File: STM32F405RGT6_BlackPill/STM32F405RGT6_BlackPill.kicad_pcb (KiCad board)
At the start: 2 copper layers, 57 parts, among them J100 Conn_01x04, J101 Conn_02x15_Odd_Even, J102 Conn_02x15_Odd_Even, J200 USB_C_Receptacle_USB2.0_16P, U100 STM32F405RGTx, U200 USBLC6-2SC6, U201 ACM2012-900-2P-T001, U300 TLV62569DBV, Y1 32768Hz, Y100 25Mhz

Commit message: Initial components placement
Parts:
- J100: footprint Connector_PinHeader_2.54mm:PinHeader_1x04_P2.54mm_Horizontal -> Connector_PinHeader_2.54mm:PinHeader_1x04_P2.54mm_Vertical
- L100, L300: value 10n -> 10nH
- moved SW101 140.4 mm to (76.1, 44.6)
- moved SW100 137.9 mm to (75.9, 60.8)
- moved SW102 133.3 mm to (82.5, 57.4), turned to 180 degrees
- moved U100 94.6 mm to (105.9, 54.7)
- moved R102 88.9 mm to (85.1, 49.7), turned to 90 degrees
- moved R107 87.8 mm to (85.0, 57.9), turned to -90 degrees
- moved Y1 87.7 mm to (90.0, 51.0), turned to 180 degrees
- moved Y100 86.8 mm to (90.0, 57.2), turned to 180 degrees
- moved R104 83.3 mm to (88.8, 54.5), turned to 180 degrees
- moved R100 82.7 mm to (84.9, 60.3), turned to 90 degrees
- moved C100 82.6 mm to (85.1, 47.5), turned to 90 degrees
- moved C113 82.3 mm to (88.8, 53.4)
- moved R103 81.2 mm to (89.0, 60.7), turned to 180 degrees
- moved C111 79.9 mm to (89.0, 59.6)
- moved C109 79.2 mm to (93.9, 56.9), turned to 90 degrees
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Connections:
- net Net-(C111-Pad1) renamed /MCU/XTAL_IN
- net Net-(C113-Pad1) renamed /MCU/XTAL32_IN
- net Net-(D101-A1) renamed /MCU/SWDIO_CONN
- net Net-(D102-A1) renamed /MCU/SWCLK_CONN
- net Net-(U100-VCAP_1) renamed /MCU/VCAP_1
- net Net-(U100-VCAP_2) renamed /MCU/VCAP_2
- C110 pad 1: HSE_OUT -> HSE_IN
- C112 pad 1: OSC32_OUT -> OSC32_IN
- R103 pad 1: HSE_IN -> HSE_OUT
- R104 pad 1: OSC32_IN -> OSC32_OUT
- Y1 pad 1: OSC32_OUT -> OSC32_IN
- Y100 pad 1: HSE_OUT -> HSE_IN
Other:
- copper layers 2 -> 4
- board text added: "BOOT0"
- board text added: "BTN PC13"
- board text added: "LED PB2"
- board text added: "NRST"

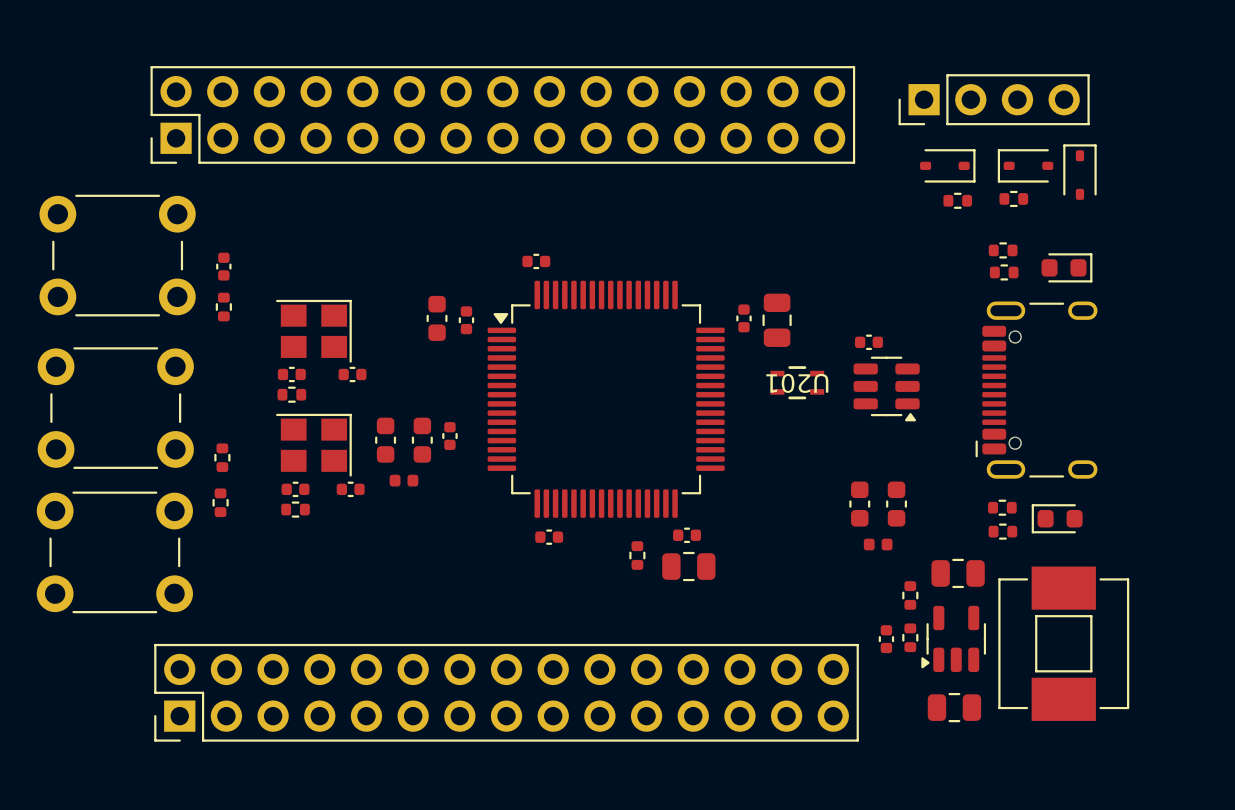
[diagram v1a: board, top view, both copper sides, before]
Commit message: Border outline
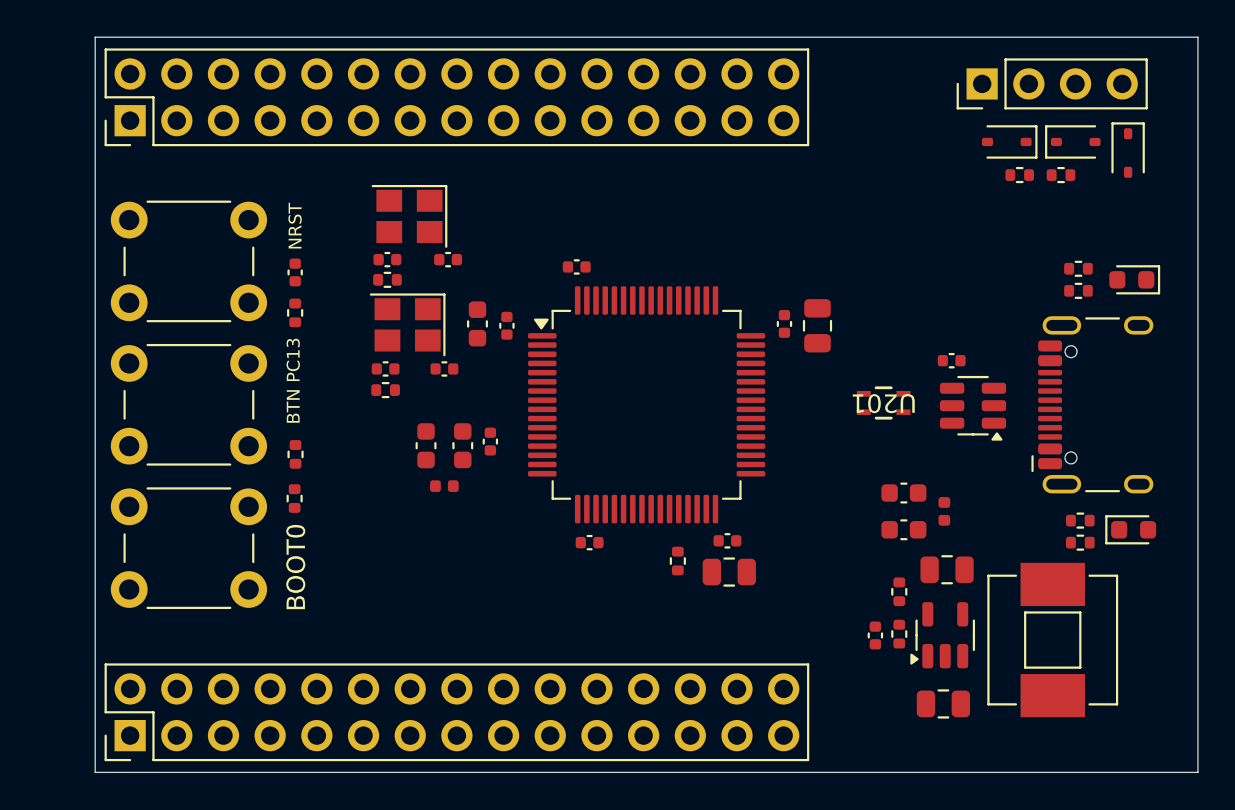
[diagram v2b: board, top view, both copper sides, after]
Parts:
- moved C110 8.30 mm to (97.1, 53.0)
- moved Y100 8.30 mm to (95.1, 50.6)
- moved C111 8.18 mm to (93.9, 53.0)
- moved R103 8.14 mm to (93.9, 54.2)
- moved C112 8.13 mm to (97.3, 47.1)
- moved C113 8.13 mm to (94.0, 47.1)
- moved R104 8.13 mm to (94.0, 48.2)
- moved Y1 8.13 mm to (95.2, 44.8)
- moved U201 4.83 mm to (121.0, 54.9)
- moved U200 4.82 mm to (125.9, 55.0)
- moved C200 4.61 mm to (124.7, 52.6)
- moved R201 4.30 mm to (131.7, 61.3)
- moved R302 4.26 mm to (131.7, 62.5)
- moved R108 4.22 mm to (131.6, 47.6)
- moved R200 4.16 mm to (131.6, 48.8)
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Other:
- board outline added: 60 x 40 mm

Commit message: Signal routing (bottom part)
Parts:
- moved SW101 22.0 mm to (79.8, 66.9), turned to 90 degrees
- moved SW100 18.0 mm to (84.2, 43.0), turned to -90 degrees
- moved R100 15.8 mm to (86.6, 44.5), turned to -90 degrees
- moved C100 15.7 mm to (86.6, 63.3)
- moved R102 15.7 mm to (86.6, 65.5)
- moved R201 12.6 mm to (131.6, 48.8)
- moved R200 12.5 mm to (131.7, 61.3)
- moved SW102 8.10 mm to (79.8, 52.7), turned to 0 degrees
- moved R107 5.61 mm to (88.5, 52.1)
- moved J102 4.40 mm to (84.4, 39.4)
- moved J101 4.38 mm to (84.4, 73.0)
- moved R101 3.47 mm to (109.4, 67.0), turned to 180 degrees
- moved R300 3.36 mm to (125.2, 67.8)
- moved C304 3.36 mm to (123.9, 67.8)
- moved L301 3.35 mm to (133.6, 67.9)
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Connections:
- C109 pad 1: +3V3 -> +3.3V
- C303 pad 1: +3V3 -> +3.3V
- C304 pad 1: +3V3 -> +3.3V
- D100 pad 1: +3V3 -> +3.3V
- D300 pad 2: +3V3 -> +3.3V
- J100 pad 4: +3V3 -> +3.3V
- J101 pad 1: +5V -> GND
- J101 pad 10: PC3 -> PA2
- J101 pad 11: PA0 -> PA5
- J101 pad 12: PA1 -> PA4
- J101 pad 13: PA2 -> PA7
- J101 pad 14: PA3 -> PA6
- J101 pad 15: PA4 -> PC5
- J101 pad 16: PA5 -> PC4
- J101 pad 17: PA6 -> PB1
- J101 pad 18: PA7 -> PB0
- J101 pad 19: PC4 -> PB11
- J101 pad 2: GND -> +3.3V
- J101 pad 20: PC5 -> PB10
- J101 pad 21: PB0 -> PB13
- J101 pad 22: PB1 -> PB12
- J101 pad 23: PB10 -> PB15
- J101 pad 24: PB11 -> PB14
- J101 pad 25: +3.3V -> PC7
- J101 pad 26: GND -> PC6
- J101 pad 27: +3.3V -> PC9
- J101 pad 28: GND -> PC8
- J101 pad 29: +3.3V -> GND
- J101 pad 3: +5V -> PC1
- J101 pad 30: GND -> +5V
- J101 pad 4: GND -> PC0
- J101 pad 5: +5V -> PC3
- J101 pad 6: GND -> PC2
- J101 pad 7: PC0 -> PA1
- J101 pad 8: PC1 -> PA0
- J101 pad 9: PC2 -> PA3
- J102 pad 19: PC9 -> unconnected-(J102-Pin_19-Pad19)
- J102 pad 20: PC8 -> unconnected-(J102-Pin_20-Pad20)
- J102 pad 21: PC7 -> unconnected-(J102-Pin_21-Pad21)
- J102 pad 22: PC6 -> unconnected-(J102-Pin_22-Pad22)
- J102 pad 23: PB15 -> unconnected-(J102-Pin_23-Pad23)
- J102 pad 24: PB14 -> unconnected-(J102-Pin_24-Pad24)
- J102 pad 25: PB13 -> unconnected-(J102-Pin_25-Pad25)
- J102 pad 26: PB12 -> unconnected-(J102-Pin_26-Pad26)
- L100 pad 2: +3V3 -> +3.3V
- L301 pad 2: +3V3 -> +3.3V
- R300 pad 2: +3V3 -> +3.3V
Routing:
- net +3.3V: track 0.00 -> 253.0 mm, vias 0 -> 12
- net PC13: track 0.00 -> 38.6 mm
- net BOOT0: track 0.00 -> 37.2 mm
- net NRST: track 0.00 -> 33.8 mm
- net GND: track 0.00 -> 32.5 mm, vias 0 -> 50
- net PC1: track 0.00 -> 30.2 mm
- net PC0: track 0.00 -> 28.4 mm
- net PC3: track 0.00 -> 27.9 mm
- net PC2: track 0.00 -> 25.9 mm
- net +5V: track 0.00 -> 25.9 mm
- net SWCLK: track 0.00 -> 24.7 mm
- net SWDIO: track 0.00 -> 24.0 mm
- net PC9: track 0.00 -> 23.9 mm
- net PC7: track 0.00 -> 22.8 mm
- net PA3: track 0.00 -> 22.7 mm
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- added copper zone on F.Cu, net +3.3V
- added copper zone on F.Cu, net +3.3VA
- added copper zone on F.Cu, net +5V
- added copper zone on F.Cu, net /power/BUCK_SW
- added copper zone on F.Cu, net GND
- added copper zone on In1.Cu, net GND
- added copper zone on In2.Cu, net GND
- added copper zone on F.Cu, net VBUS
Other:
- rule pad_to_mask_clearance: 0 -> 0.038

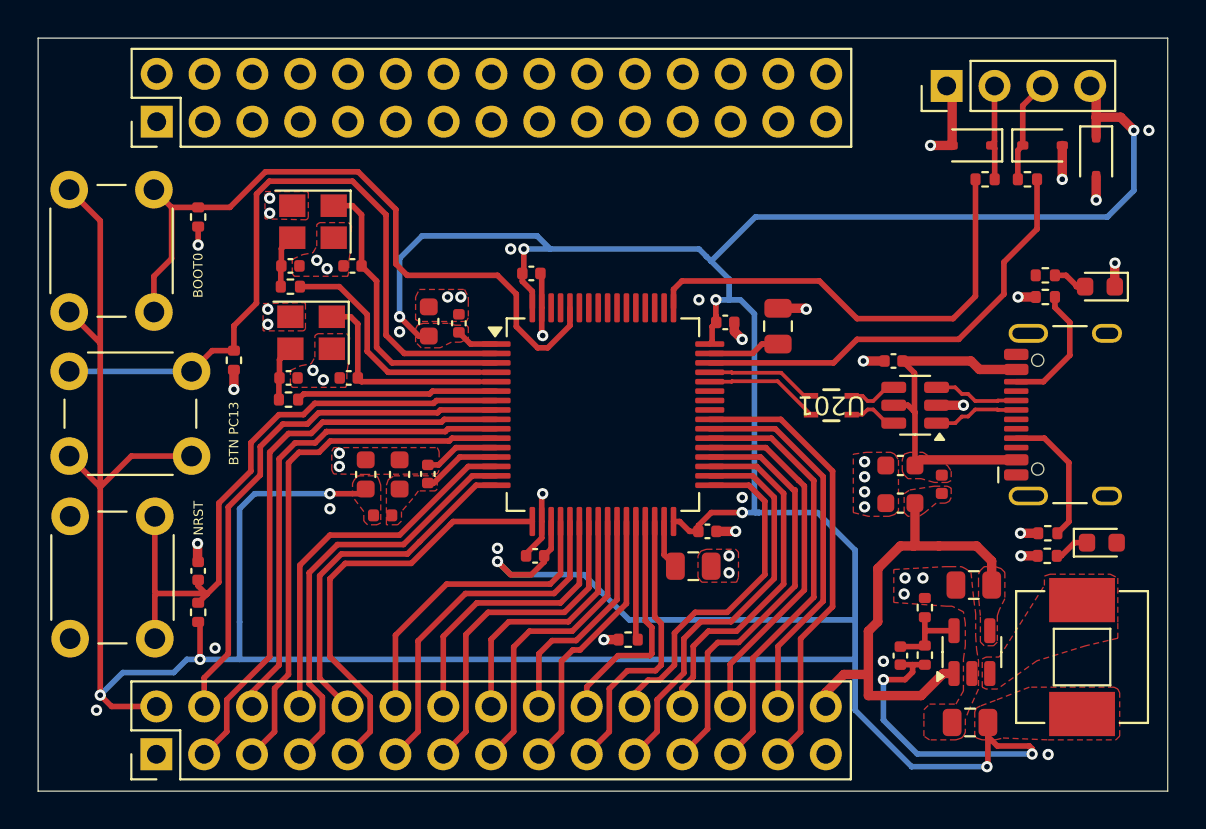
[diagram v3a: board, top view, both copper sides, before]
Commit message: Signal routing (upper part)
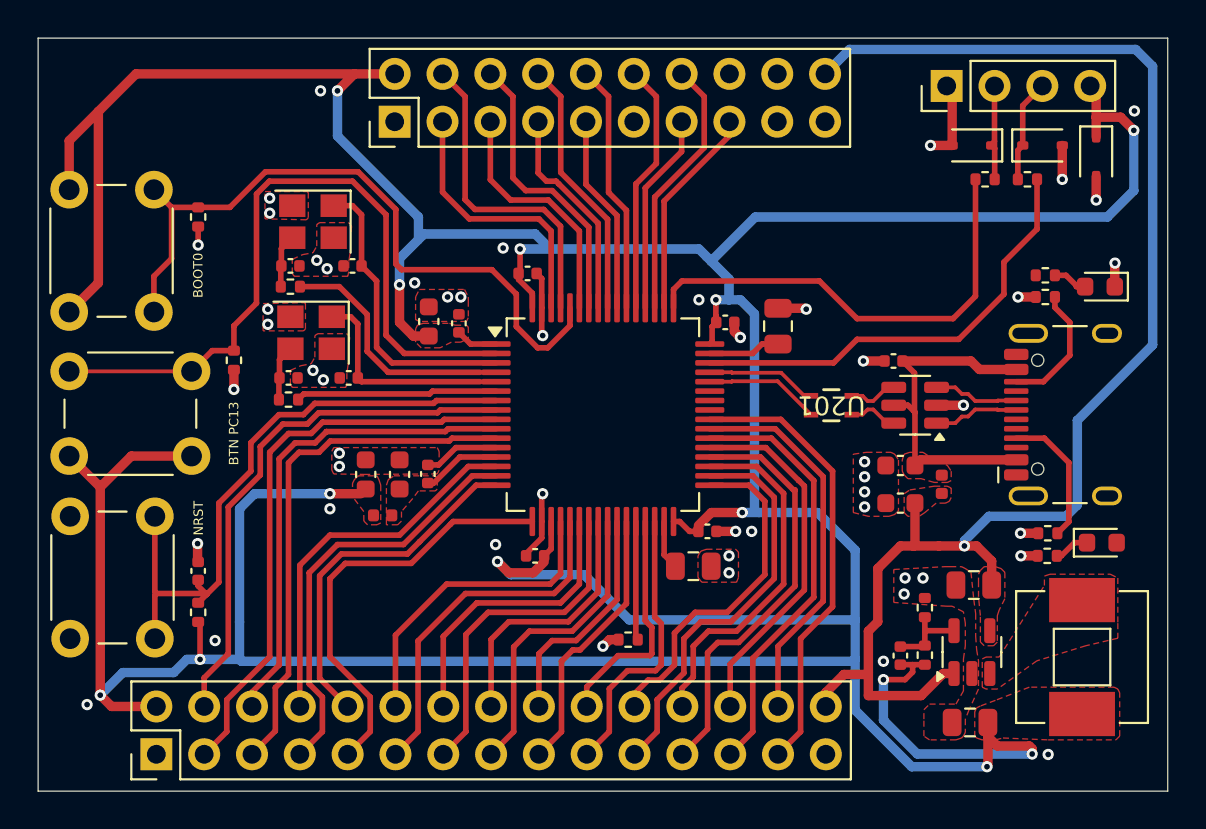
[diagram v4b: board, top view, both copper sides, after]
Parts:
- J102: value Conn_02x15_Odd_Even -> Conn_02x10_Odd_Even; footprint Connector_PinHeader_2.54mm:PinHeader_2x15_P2.54mm_Vertical -> Connector_PinHeader_2.54mm:PinHeader_2x10_P2.54mm_Vertical
- moved J102 12.6 mm to (97.0, 39.4)
- moved C103 0.20 mm to (104.1, 47.5)
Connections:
- J102 pad 1: +5V -> GND
- J102 pad 11: PC11 -> GND
- J102 pad 13: PA15 -> PC11
- J102 pad 15: PA9 -> PA15
- J102 pad 17: GND -> PA9
- J102 pad 19: unconnected-(J102-Pin_19-Pad19) -> GND
- J102 pad 2: GND -> +3.3V
- J102 pad 20: unconnected-(J102-Pin_20-Pad20) -> +5V
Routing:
- net +5V: track 25.9 -> 76.2 mm, vias 0 -> 1
- net +3.3V: track 253.0 -> 278.1 mm, vias 12 -> 13
- net PB8: track 0.00 -> 17.2 mm
- net PB6: track 0.00 -> 15.4 mm
- net PB9: track 0.00 -> 14.4 mm
- net PC10: track 0.00 -> 14.0 mm
- net PB4: track 0.00 -> 14.0 mm
- net PC12: track 0.00 -> 13.4 mm
- net PD2: track 0.00 -> 13.3 mm
- net PB7: track 0.00 -> 13.0 mm
- net PB5: track 0.00 -> 11.5 mm
- net PA15: track 0.00 -> 11.3 mm
- net PC11: track 0.00 -> 10.7 mm
- net PB3: track 0.00 -> 10.6 mm
- net GND: track 32.5 -> 32.6 mm, vias 50 -> 51

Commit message: Minor DCR fixes
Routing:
- net +3.3V: track 278.1 -> 299.8 mm
- net /USB/USB_CONN_D+: track 4.54 -> 7.46 mm
- net /USB/USB_CONN_D-: track 4.54 -> 6.69 mm
- net SWCLK: track 24.7 -> 23.6 mm
- net SWDIO: track 24.0 -> 23.0 mm
- net GND: vias 51 -> 55

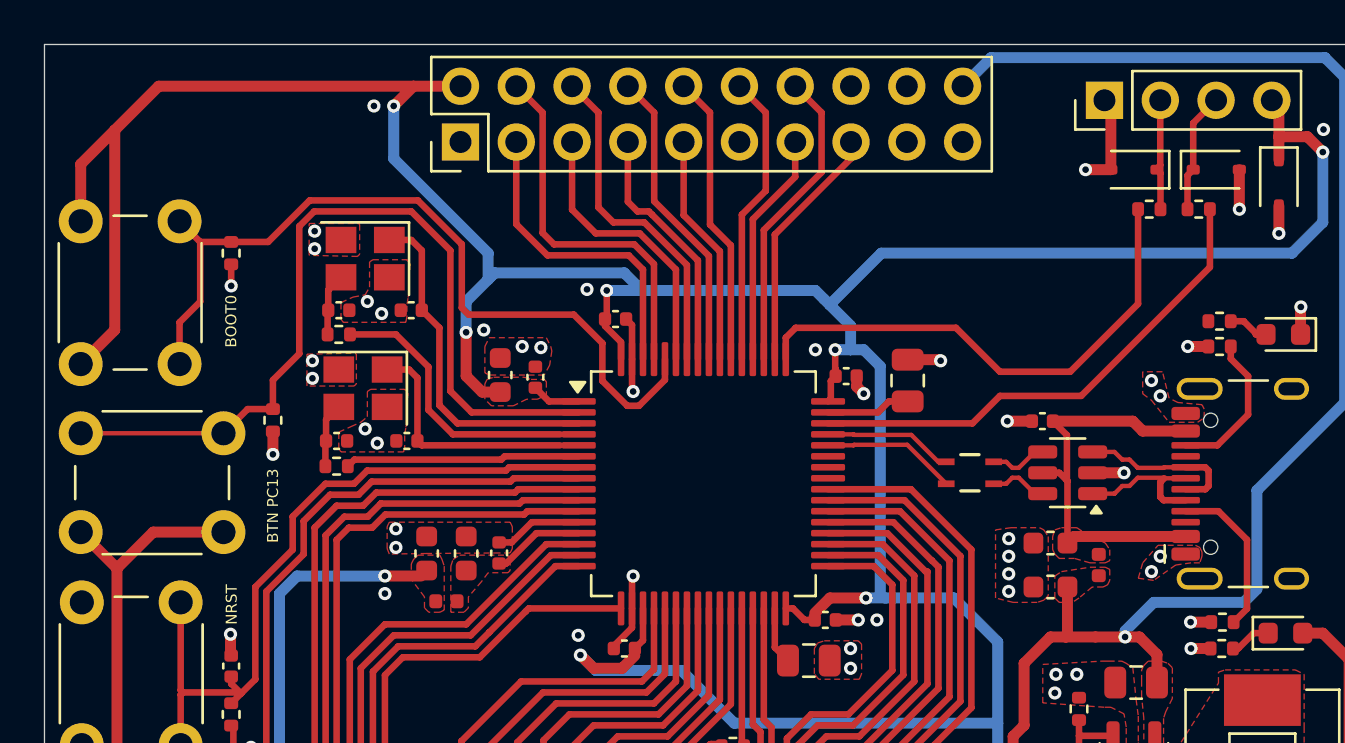
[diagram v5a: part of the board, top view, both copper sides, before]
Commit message: All signals routed
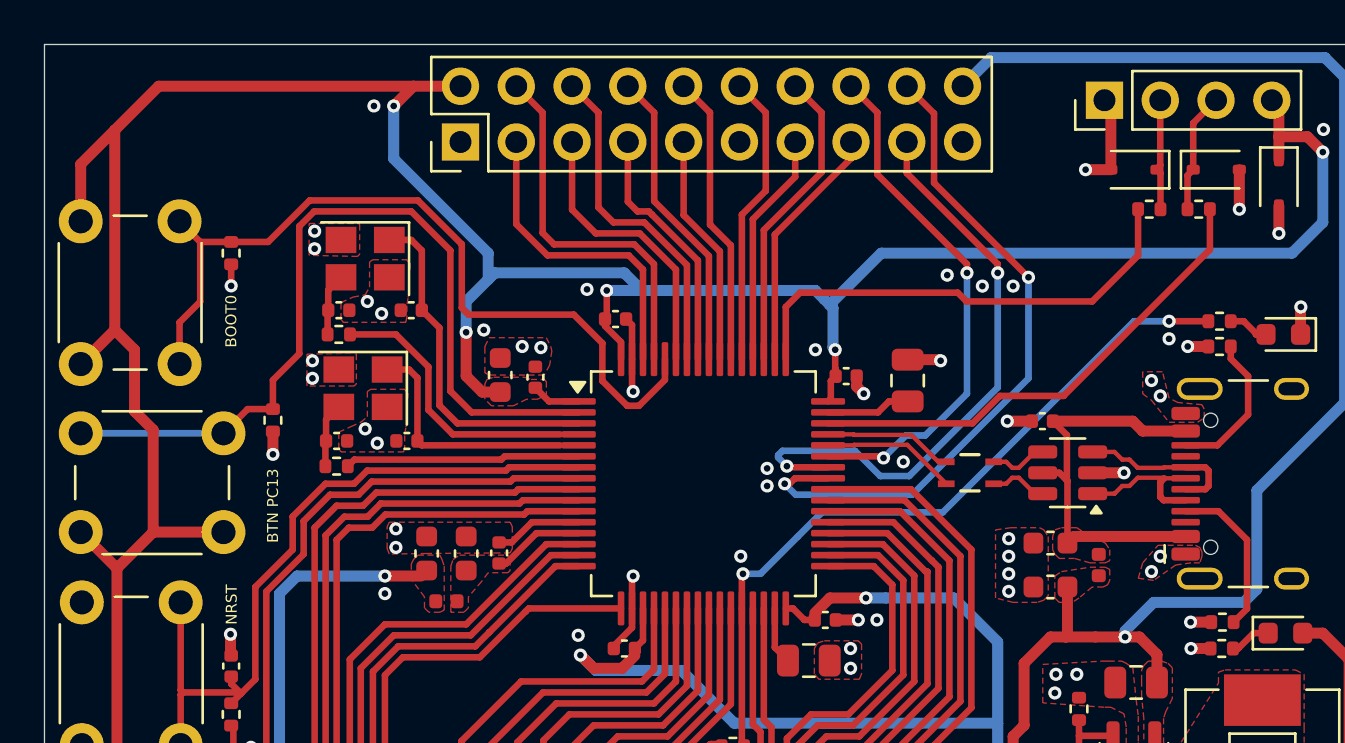
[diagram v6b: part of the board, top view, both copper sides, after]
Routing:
- net PA8: track 0.00 -> 31.2 mm, vias 0 -> 2
- net PA9: track 0.00 -> 27.7 mm, vias 0 -> 2
- net PB2: track 6.32 -> 33.9 mm, vias 0 -> 2
- net PA10: track 0.00 -> 23.8 mm, vias 0 -> 2
- net +3.3V: track 299.8 -> 296.6 mm
- net SWCLK: track 23.6 -> 21.8 mm
- net GND: vias 55 -> 63
